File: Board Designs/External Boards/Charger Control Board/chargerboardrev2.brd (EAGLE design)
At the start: 160 x 100 mm, 20 parts, among them J1 JUMPER.1, X1 CONNECTOR-6NANO-FIT_VERTICAL-6, X3 CONNECTOR-2, X4 CONNECTOR-2

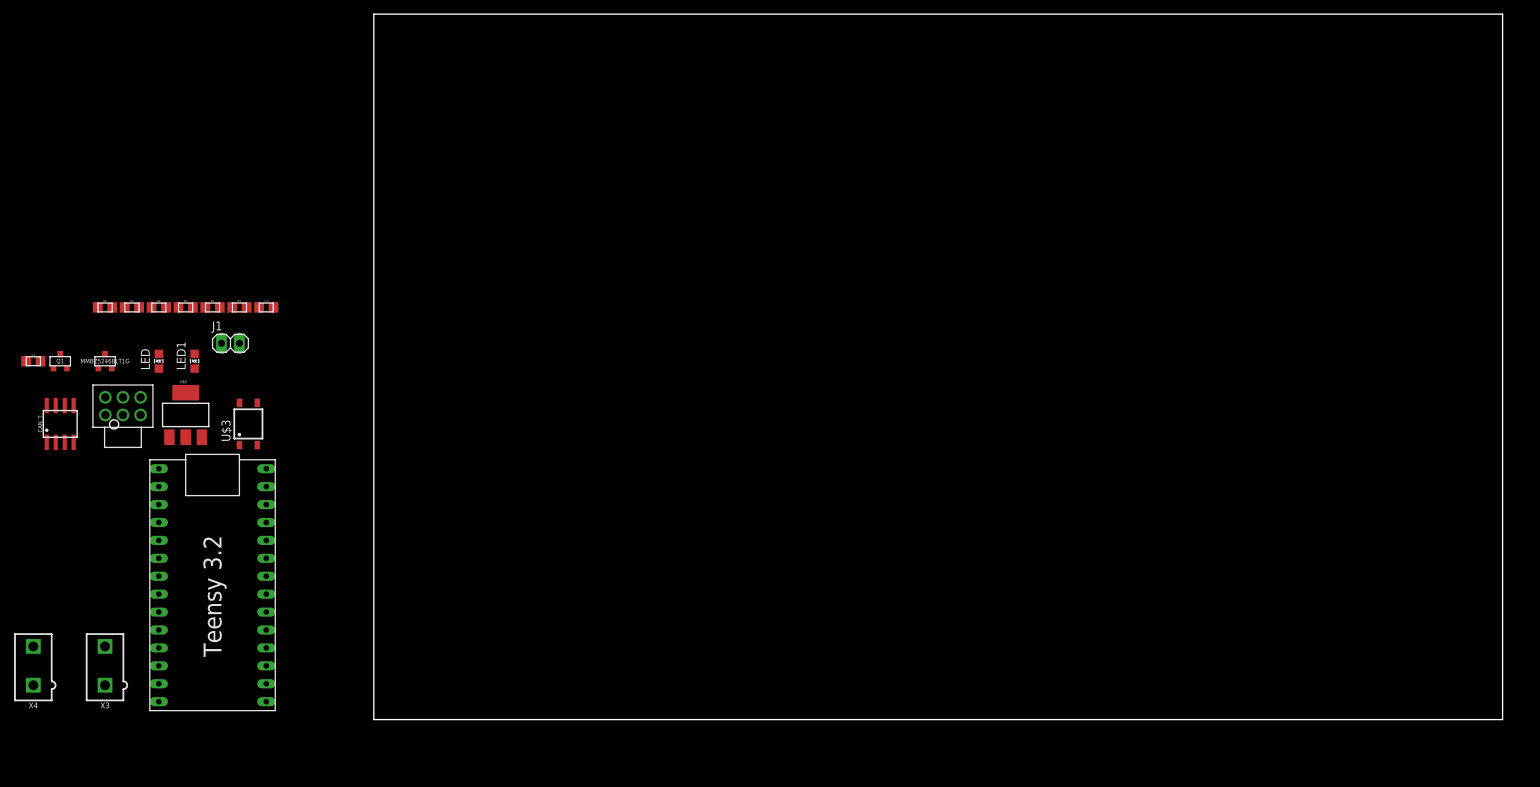
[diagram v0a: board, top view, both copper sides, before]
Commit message: Adjusted schematic for v2 of charger control board
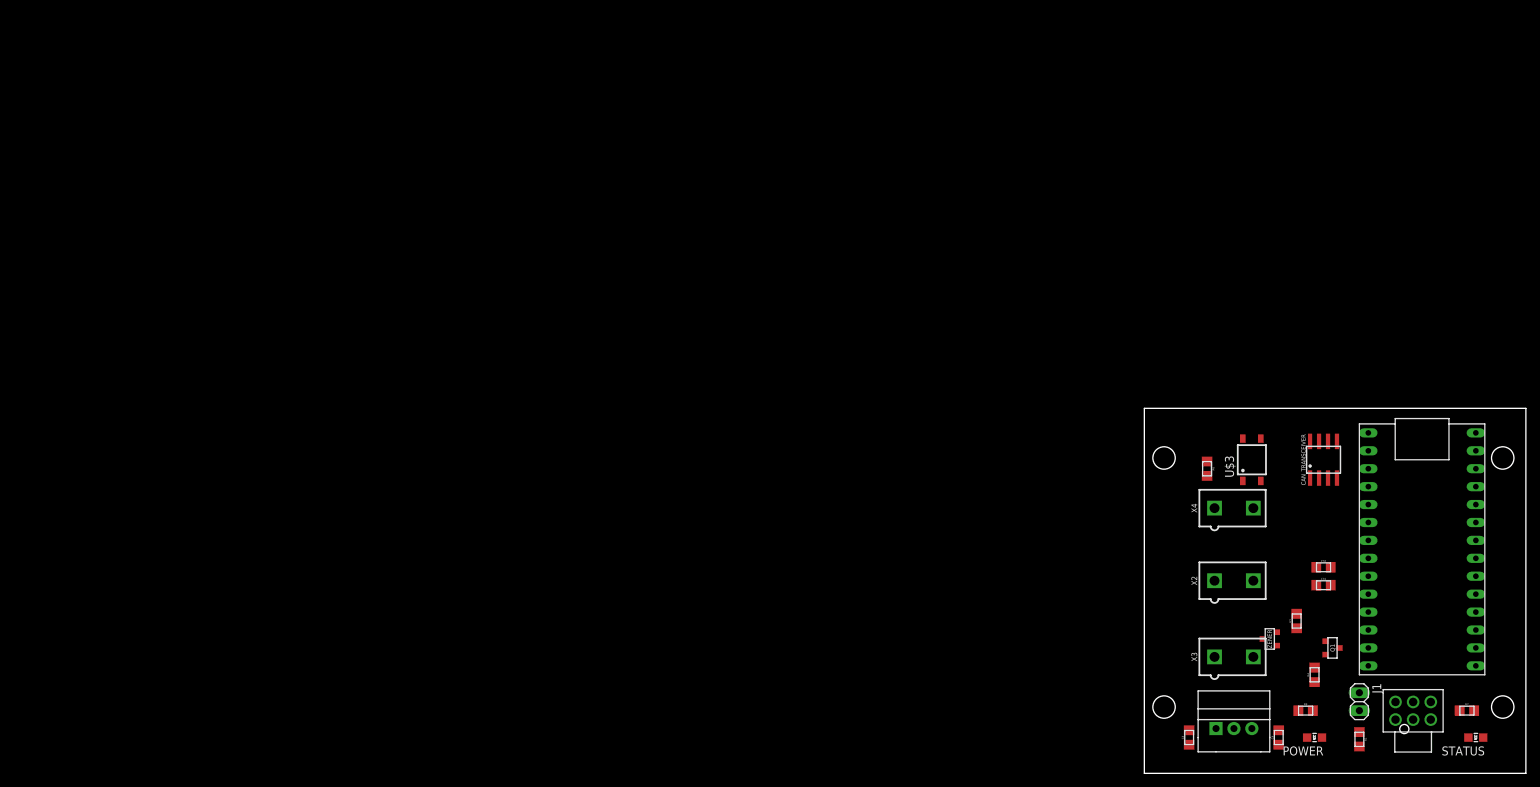
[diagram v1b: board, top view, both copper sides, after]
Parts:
- removed C1, C2: 0.22uF, HyTechDevices:0805
- removed CAN_T: MCP2551, HyTechDevices:SOIC-08
- removed LED, LED1: (no value), HyTechDevices:LED-805
- removed MMBZ5246BLT1G: DIODE_ZENER, HyTechDevices:SOT23
- removed R2, R5: 1.2k, HyTechDevices:0805
- removed U$1: TEENSY_3.2_SIMPLE, HyTechDevices:TEENSY_3.2_SIMPLE
- removed U$2: (no value), HyTechDevices:SOT223
- added C3, C4: 10uF, HyTechDevices:0805
- added C31: 1uF, HyTechDevices:0805
- added C32: .1uF, HyTechDevices:0805
- added CAN_TRANSCEIVER: MCP2551, HyTechDevices:SOIC-08
- added POWER: GREEN, HyTechDevices:LED-805
- added R7: 68, HyTechDevices:0805
- added R8: 200, HyTechDevices:0805
- added REG: 5V, HyTechDevices:OKI-78SR
- added STATUS: RED, HyTechDevices:LED-805
- added U$4: TEENSY_3.2_SIMPLE, HyTechDevices:TEENSY_3.2_SIMPLE
- added X2: Shutdown Button, HyTechDevices:MINIFIT_5566-2
- added ZENER: (no value), HyTechDevices:SOT23
- R3: value 20k -> 40k
- R6: value 330 -> 360
- X1: value CONNECTOR-6NANO-FIT_VERTICAL-6 -> Car Connector
- X3: value CONNECTOR-2 -> Powerswitch Tail
- X4: value CONNECTOR-2 -> Charge Toggle
- moved X1 187.9 mm to (147.3, 0.00)
- moved Q1 184.9 mm to (135.9, 10.2), turned to 270 degrees
- moved R4 171.9 mm to (133.3, 6.35), turned to 90 degrees
- moved X4 171.6 mm to (121.9, 30.0), turned to 270 degrees
- moved R1 170.1 mm to (139.7, -2.79), turned to 270 degrees
- moved J1 167.9 mm to (139.7, 2.54), turned to 270 degrees
- moved R3 163.6 mm to (130.8, 14.0), turned to 90 degrees
- moved X3 160.0 mm to (121.9, 8.89), turned to 270 degrees
- moved R6 157.9 mm to (118.1, 35.6), turned to 270 degrees
- moved U$3 142.3 mm to (124.5, 36.8)
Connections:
- removed net 12V: C1.1, U$2.1, U$3.4, X1.P$1
- removed net 5V: C2.1, CAN_T.3, U$1.VIN, U$2.3, X3.1
- removed net CANRX: CAN_T.4, U$1.D4(CANRX)
- removed net CANTX: CAN_T.1, U$1.D3(CANTX)
- removed net CHARGE_ENABLE: MMBZ5246BLT1G.3, R3.2, X1.P$3
- removed net CHRG_C: R6.1, U$1.D0(RX1)
- removed net N$2: R2.2, U$1.D11
- removed net N$3: R5.1, U$1.D8(TX3)
- removed net N$4: LED1.A, R2.1
- removed net N$6: LED.A, R5.2
- removed net SIGNAL_SAFE: Q1.1, R3.1, R4.2, U$1.A0
- new net +12V: C3.2, REG.1, U$3.4, X1.P$1
- new net +5V: C31.2, C32.2, C4.2, CAN_TRANSCEIVER.3, R8.1, REG.3, U$4.VIN, X3.1
- new net CHARGER_ON: Q1.1, R3.1, R4.2, U$4.A0
- new net N$11: R7.2, U$4.D8(TX3)
- new net N$15: CAN_TRANSCEIVER.4, U$4.D4(CANRX)
- new net N$22: CAN_TRANSCEIVER.1, U$4.D3(CANTX)
- new net N$8: R7.1, STATUS.A
- new net N$9: POWER.A, R8.2
- new net SHUTDOWN_CIRCUIT: R3.2, X1.P$3, X2.1, X2.2, ZENER.3
- new net TOGGLE_CHARGER: R6.1, U$4.D0(RX1)
- net CANH: now also CAN_TRANSCEIVER.7; no longer CAN_T.7
- net CANL: now also CAN_TRANSCEIVER.6; no longer CAN_T.6
- net GND: now also C3.1, C31.1, C32.1, C4.1, CAN_TRANSCEIVER.2, CAN_TRANSCEIVER.8, POWER.C, REG.2, STATUS.C, U$4.GND, ZENER.1; no longer C1.2, C2.2, CAN_T.2, CAN_T.8, LED.C, LED1.C, MMBZ5246BLT1G.1, U$1.GND, U$2.2, U$2.4
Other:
- board size 160 x 100 mm -> 54.1 x 51.7 mm
- board text added: "CHARGER POWER"
- board text added: "Designed by: Dean Plaskon Arvind Srinivasan"
- board text added: "HyTech Racing 2020 Charger Board Rev2"
- board text added: "SHUTDOWN BUTTON"
- board text added: "TOGGLE CHARGER"

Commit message: Finished charger control board rev 2
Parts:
- removed C31: 1uF, HyTechDevices:0805
- removed C32: .1uF, HyTechDevices:0805
- removed J1: JUMPER.1, HyTechDevices:1X02
- removed R8: 200, HyTechDevices:0805
- added C1: 1uF, HyTechDevices:0805
- added C2: .1uF, HyTechDevices:0805
- added C5: 4.7nF, HyTechDevices:0805
- added CAN_TERM_JMP: M02_SLIM, HyTechDevices:1X02_SLIM
- added R2: 60, HyTechDevices:0805
- added R5: 200, HyTechDevices:0805
- added U$13: CDSOT23-T24CAN-Q, HyTechDevices:SOT23
- added ZENER1: DIODE, HyTechDevices:0805_D
- R1: value 120 -> 60
- moved ZENER 13.5 mm to (134.6, 22.5)
- moved R1 11.8 mm to (129.5, 3.30), turned to 90 degrees
- moved Q1 8.98 mm to (134.6, 19.1)
- moved R3 3.81 mm to (134.6, 14.0)
- moved R4 3.72 mm to (134.6, 9.84)
- moved STATUS 1.71 mm to (154.5, -2.54)
- moved CAN_TRANSCEIVER 1.52 mm to (133.1, 36.8)
- moved C3 1.14 mm to (114.9, -1.59)
- moved C4 1.14 mm to (128.9, -1.59)
- moved POWER 0.63 mm to (133.3, -3.17)
- moved R7 0.45 mm to (154.6, 1.59), turned to 180 degrees
- turned U$3 to 180 degrees
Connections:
- removed net N$5: J1.1, R1.2
- new net N$17: CAN_TERM_JMP.2, R2.2
- new net N$62: C5.1, R1.2, R2.1
- new net PRE_BRB_SHUTDOWN_CIRCUIT: X1.P$3, X2.2
- new net PRE_DIODE_CHARGER_ON: U$4.A0, ZENER1.C
- net +5V: now also C1.2, C2.2, R5.1; no longer C31.2, C32.2, R8.1
- net CANH: now also CAN_TERM_JMP.1, U$13.2; no longer J1.2
- net CANL: now also U$13.1
- net CHARGER_ON: now also ZENER1.A; no longer U$4.A0
- net GND: now also C1.1, C2.1, C5.2, U$13.3; no longer C31.1, C32.1
- net N$9: now also R5.2; no longer R8.2
- net SHUTDOWN_CIRCUIT: no longer X1.P$3, X2.2
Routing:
- net GND: track 0.00 -> 184.8 mm, vias 0 -> 2
- net +12V: track 0.00 -> 85.3 mm
- net +5V: track 0.00 -> 83.0 mm, vias 0 -> 1
- net CANL: track 0.00 -> 71.2 mm, vias 0 -> 5
- net CANH: track 0.00 -> 59.4 mm, vias 0 -> 2
- net PRE_BRB_SHUTDOWN_CIRCUIT: track 0.00 -> 55.6 mm, vias 0 -> 1
- net TOGGLE_CHARGER: track 0.00 -> 28.7 mm
- net SHUTDOWN_CIRCUIT: track 0.00 -> 26.1 mm, vias 0 -> 2
- net PRE_DIODE_CHARGER_ON: track 0.00 -> 22.3 mm, vias 0 -> 1
- net N$11: track 0.00 -> 21.6 mm
- net N$1: track 0.00 -> 17.8 mm
- net N$22: track 0.00 -> 15.1 mm, vias 0 -> 1
- net CHARGER_ON: track 0.00 -> 14.6 mm, vias 0 -> 2
- net N$62: track 0.00 -> 14.1 mm
- net N$15: track 0.00 -> 10.4 mm, vias 0 -> 1
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
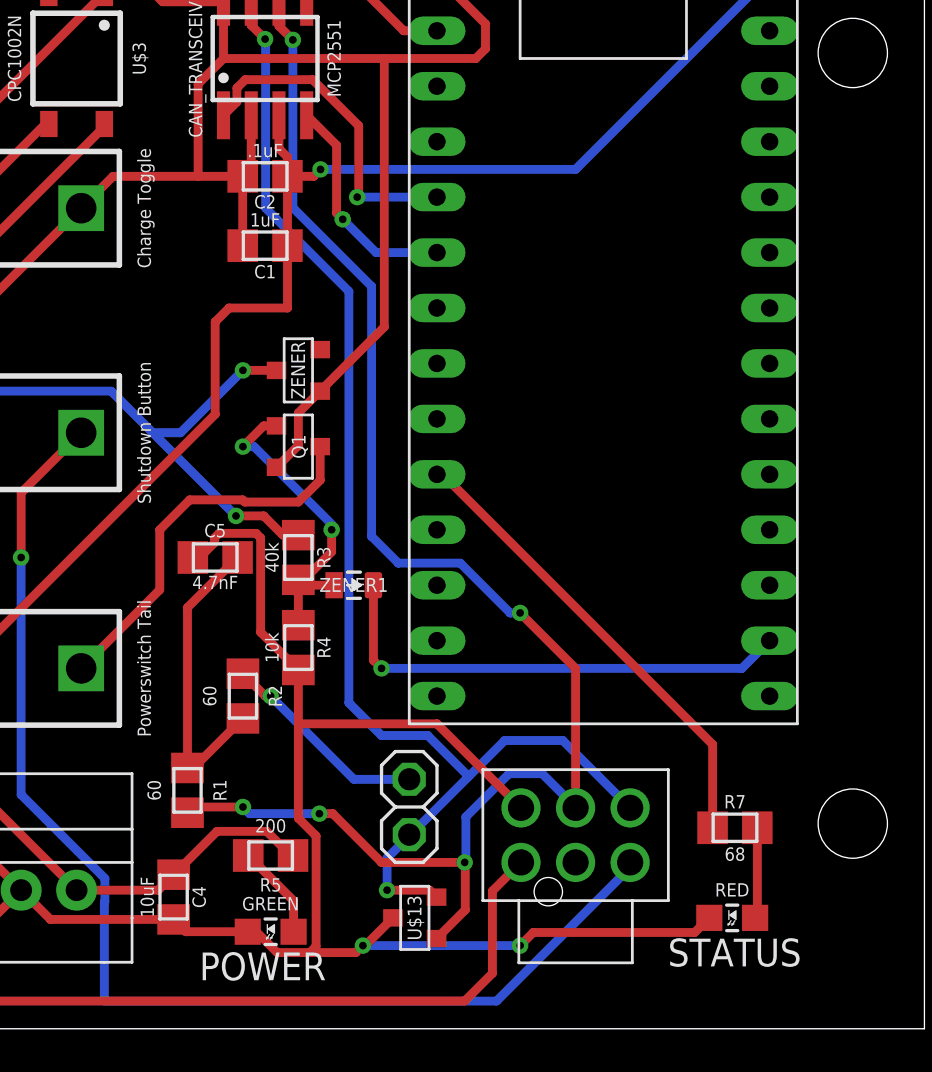
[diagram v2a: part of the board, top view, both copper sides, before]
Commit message: Fixed small board issues and exported gerbers
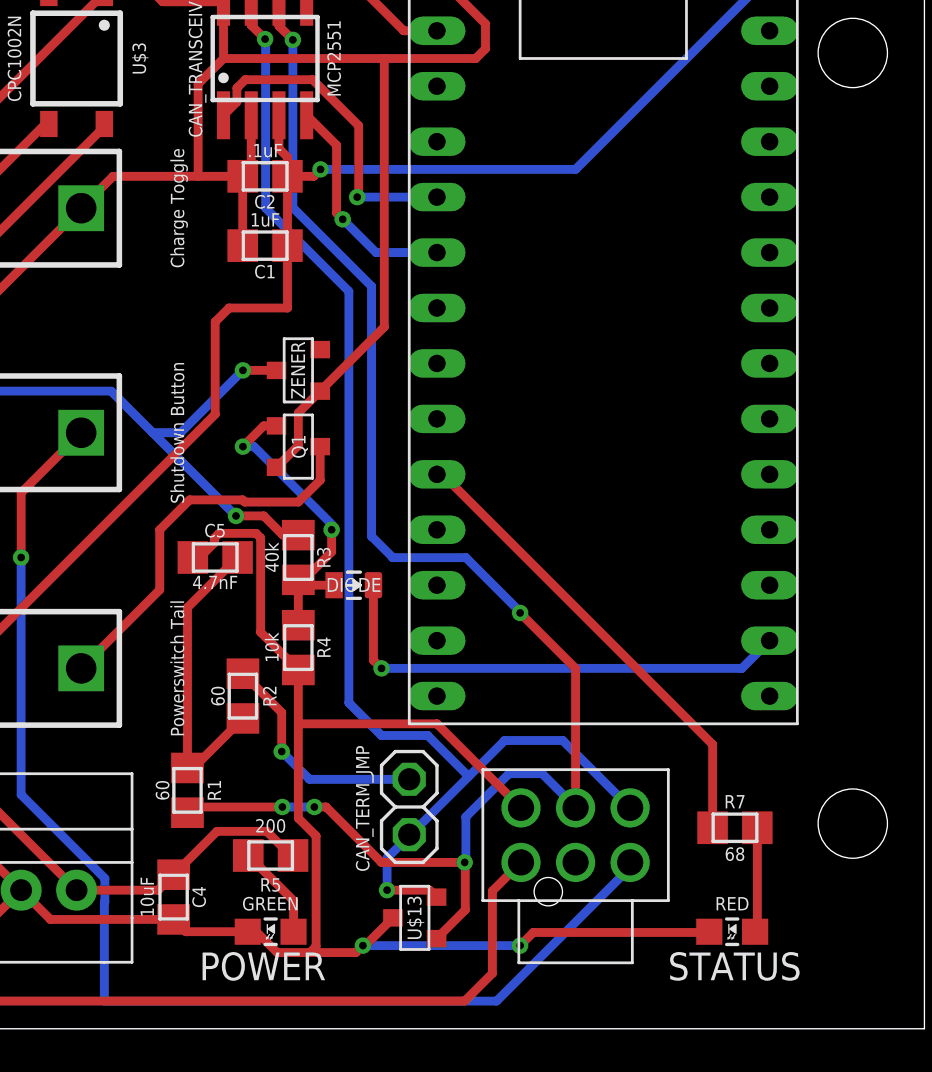
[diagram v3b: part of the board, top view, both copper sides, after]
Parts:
- moved STATUS 0.63 mm to (154.5, -3.17)
- renumbered ZENER1 to DIODE
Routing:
- net N$17: track 9.62 -> 10.7 mm
- net N$8: track 4.17 -> 4.78 mm
